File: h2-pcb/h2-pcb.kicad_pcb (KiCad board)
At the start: 2 copper layers, 123 x 74.8 mm, 102 parts, among them J1 Network Connector, J10 Temp Sensor Conn 3, J11 Actuator Connector 4, J12 Manometer Connector 3, J2 STDC14, J3 Manometer Connector 1, J4 Manometer Connector 2, J5 Actuator Connector 1, J6 Actuator Connector 2, J7 Actuator Connector 3, J8 Temp Sensor Conn 1, J9 Temp Sensor Conn 2, Q1 NMOS, Q2 PMOS, Q3 NMOS, Q4 PMOS, Q5 NMOS, Q6 PMOS, Q7 NMOS, Q8 PMOS, SW1 SW_Push, U1 LD39050PU33R, U2 STM32G474RBT6, U3 SN65HVD230, U4 DS2484, Y1 8MHz

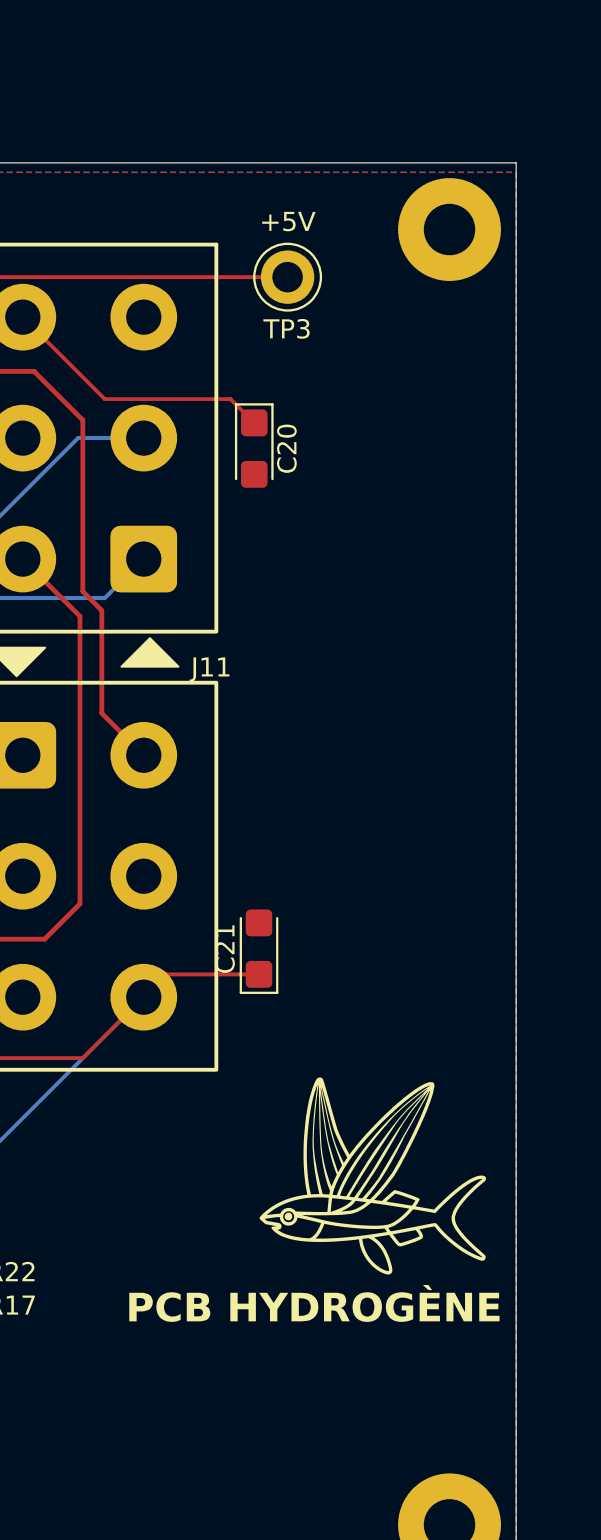
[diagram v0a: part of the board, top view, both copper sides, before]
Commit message: h2-pcb: update metadata and silkscreen
- Update author, pcb code, version and date metadata
- Add version and code to PCB name in silkscreen
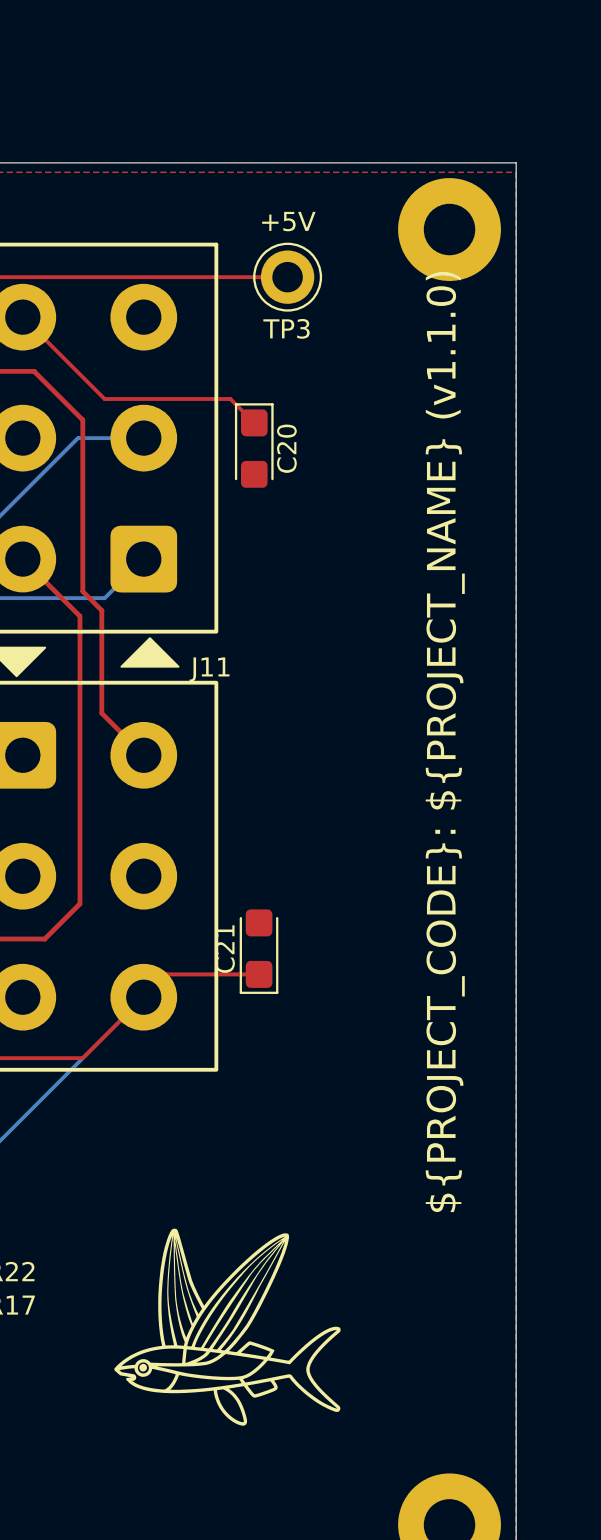
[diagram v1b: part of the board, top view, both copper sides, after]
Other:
- board text added: "${PROJECT_CODE}: ${PROJECT_NAME} (${REVISION})"
- board text removed: "PCB HYDROGÈNE"

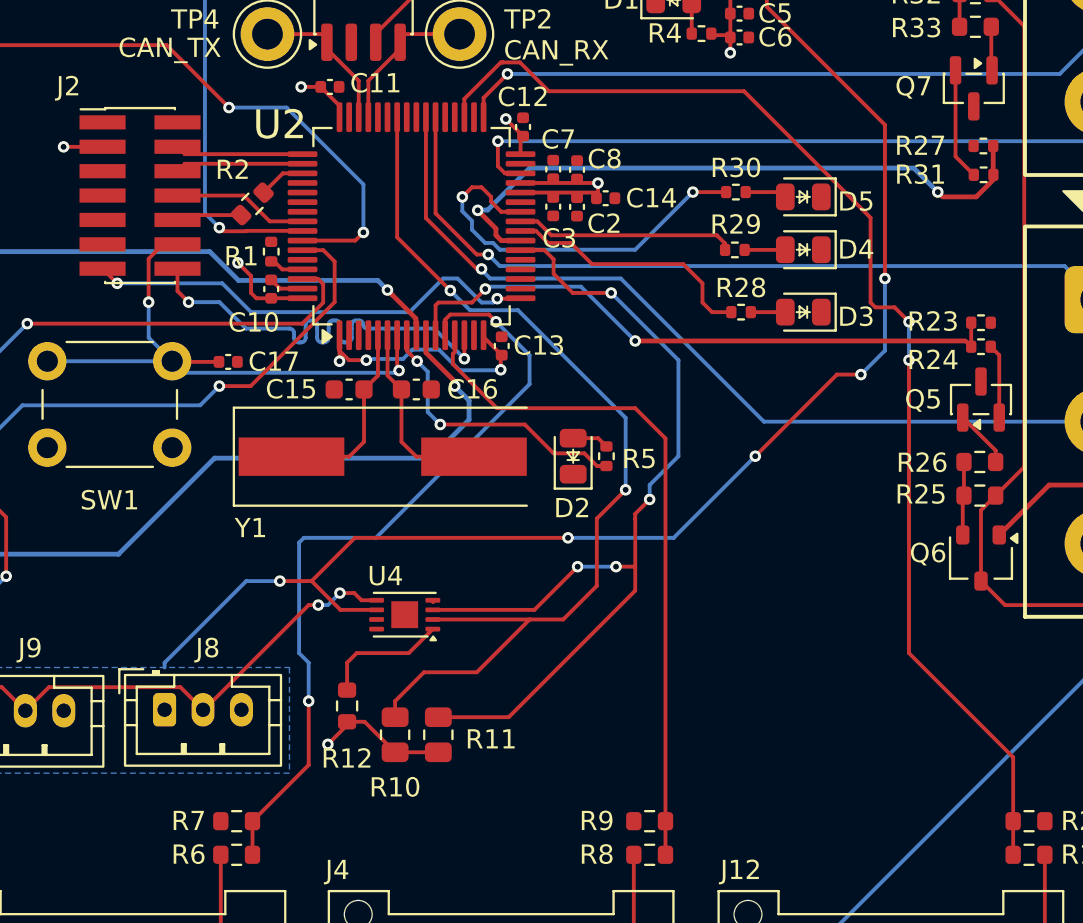
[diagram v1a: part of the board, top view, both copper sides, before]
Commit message: h2-pcb: make i2c traces parallel
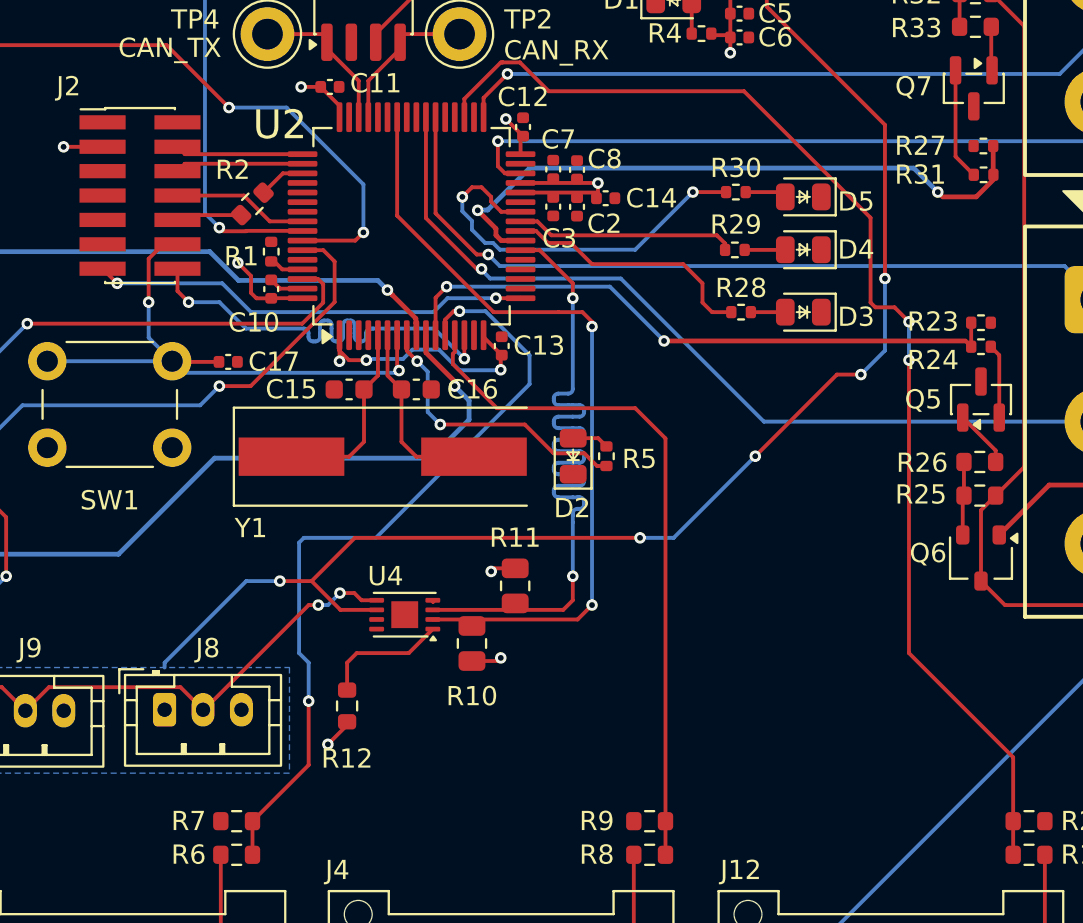
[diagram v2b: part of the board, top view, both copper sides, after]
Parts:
- moved R11 8.72 mm to (106.8, 95.0), turned to -90 degrees
- moved R10 6.21 mm to (104.5, 98.0)
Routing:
- net /SDA_TEMP: track 50.8 -> 40.9 mm
- net /SCL_TEMP: track 48.4 -> 40.8 mm, vias 4 -> 2
- net +3.3V: track 50.7 -> 48.0 mm, vias 11 -> 13
- net /STM32 Base Layout/T_VCP_RX: track 24.3 -> 23.3 mm
- net /STM32 Base Layout/T_VCP_TX: track 24.1 -> 23.2 mm

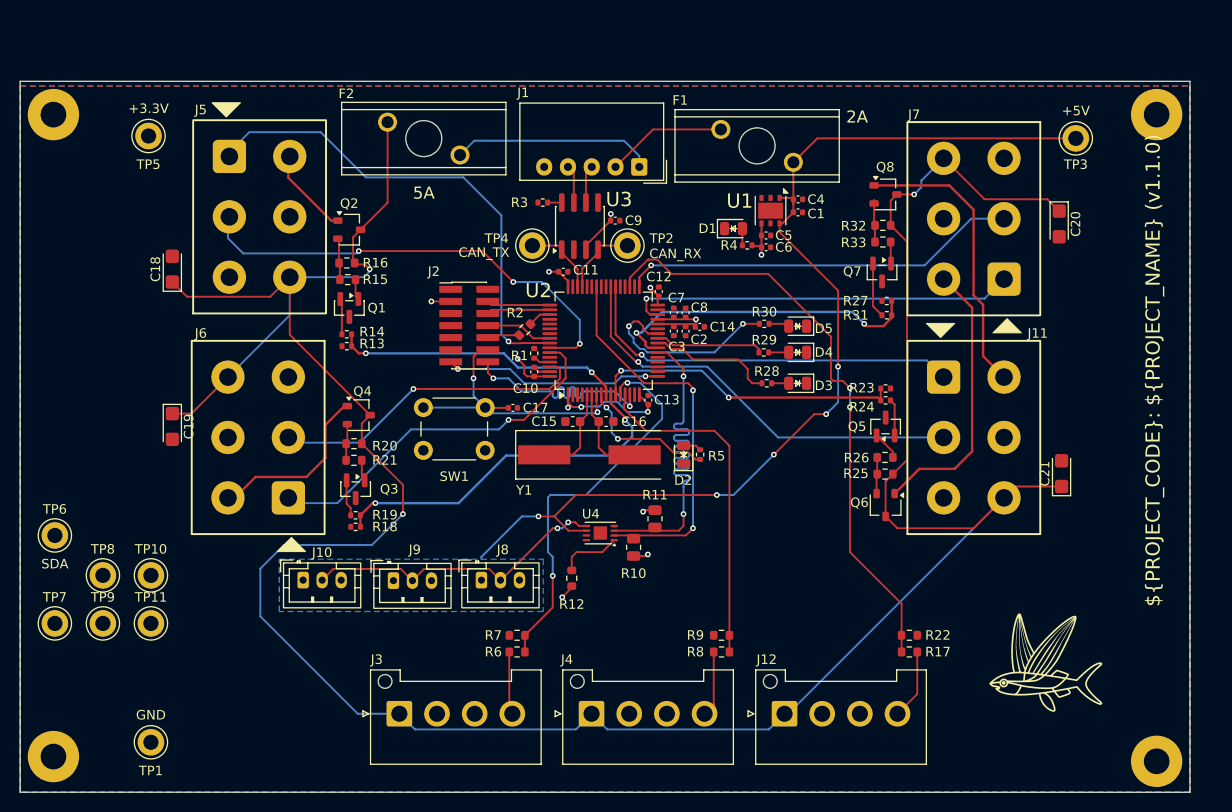
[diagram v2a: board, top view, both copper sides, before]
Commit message: Ajout des noms des composantes, routage des test points, 24V plane pour les manometres,  mounting holes 4mm de distance du edge
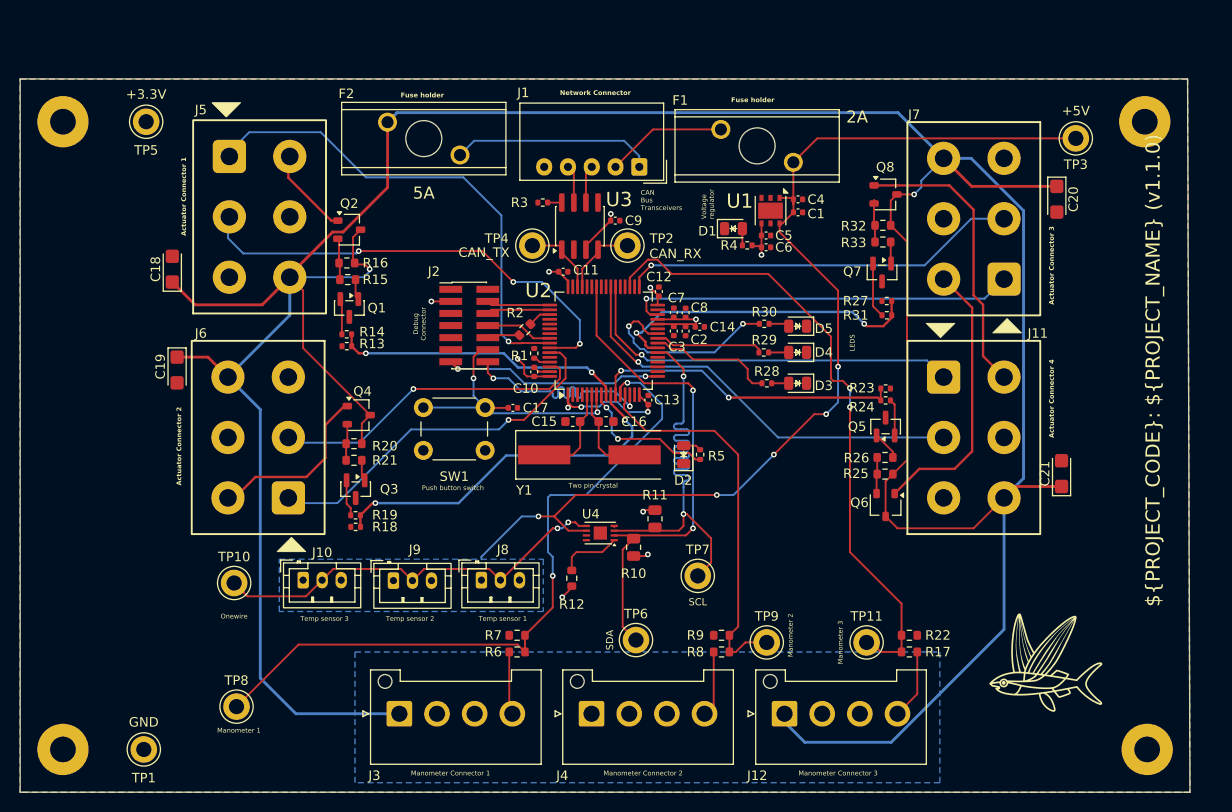
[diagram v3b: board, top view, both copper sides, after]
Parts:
- moved TP11 75.3 mm to (129.0, 108.0)
- moved TP9 69.8 mm to (118.5, 108.0)
- moved TP7 67.8 mm to (111.2, 101.0)
- moved TP6 62.1 mm to (104.8, 107.8)
- moved TP8 19.7 mm to (62.8, 114.8)
- moved TP10 8.79 mm to (62.5, 101.8)
- moved C19 5.96 mm to (56.5, 79.4)
- moved C20 2.61 mm to (149.0, 61.4)
- moved H3 1.60 mm to (158.5, 119.2)
- moved TP5 1.52 mm to (53.2, 53.2)
- moved H2 1.46 mm to (158.2, 53.2)
- moved H1 1.25 mm to (44.5, 53.2)
- moved H4 1.25 mm to (44.5, 119.2)
- moved TP1 1.06 mm to (53.0, 119.2)
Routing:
- net +24V: track 288.0 -> 364.0 mm, vias 3 -> 2
- net /MANOMETER_1: track 40.9 -> 74.7 mm
- net /SDA_TEMP: track 40.9 -> 52.6 mm
- net /ONEWIRE: track 32.4 -> 43.0 mm
- net /SCL_TEMP: track 40.8 -> 49.2 mm
- net /MANOMETER_2: track 35.9 -> 41.0 mm
- net /MANOMETER_3: track 63.1 -> 67.2 mm
- added copper zone on B.Cu, net +24V
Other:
- board size 123 x 74.8 mm -> 123 x 75 mm
- board text added: "Actuator Connector 1"
- board text added: "Actuator Connector 2"
- board text added: "Actuator Connector 3"
- board text added: "Actuator Connector 4"
- board text added: "CAN Bus Transceivers"
- board text added: "Debug Connector"
- board text added: "Fuse holder"
- board text added: "LEDS"
- board text added: "Manometer 1"
- board text added: "Manometer 2"
- board text added: "Manometer 3"
- board text added: "Manometer Connector 1"
- board text added: "Manometer Connector 2"
- board text added: "Manometer Connector 3"
- board text added: "Network Connector"
- board text added: "Onewire"
- board text added: "Push button switch"
- board text added: "SCL"
- board text added: "SDA"
- board text added: "Temp sensor 1"
- board text added: "Temp sensor 2"
- board text added: "Temp sensor 3"
- board text added: "Two pin crystal"
- board text added: "Voltage regulator"

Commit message: h2-pcb: replace ds2484 symbol
The symbol is now the one from the official KiCad library. PCB was also
updated and any remaining DRC errors were fixed.
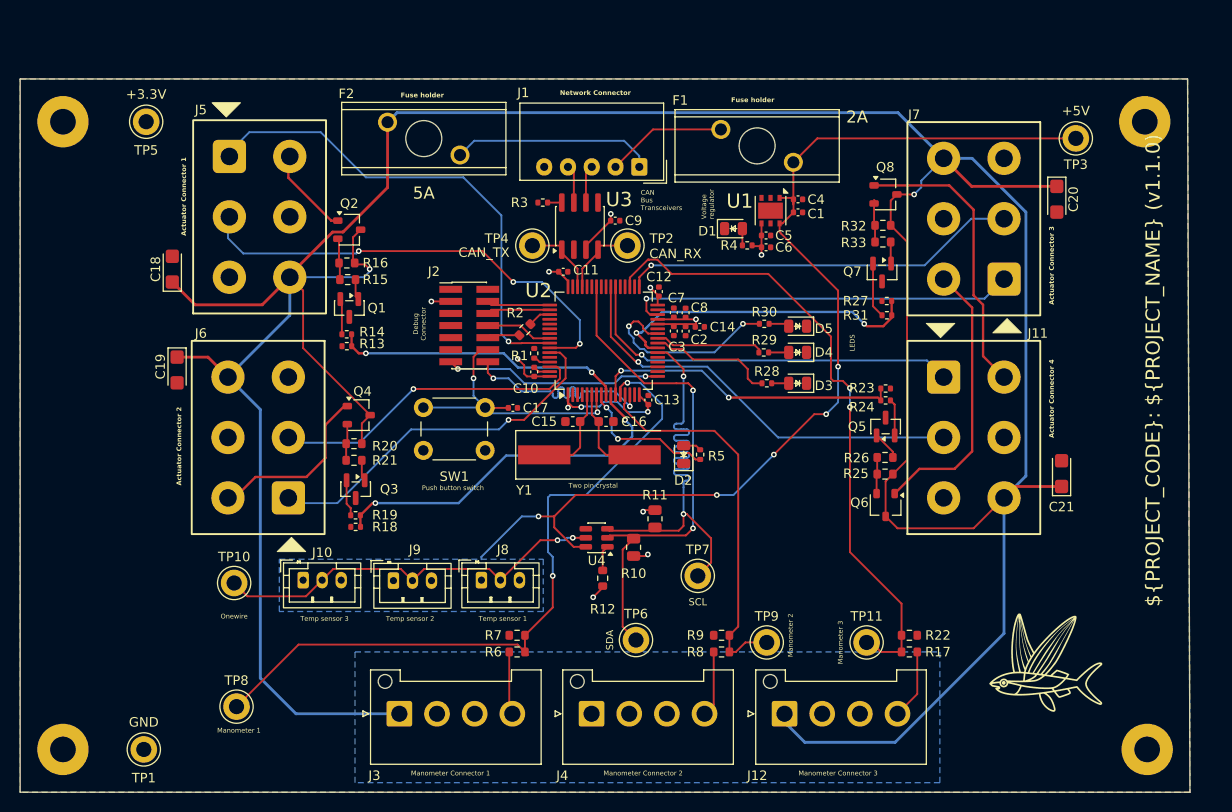
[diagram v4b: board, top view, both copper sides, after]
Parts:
- U4: value DS2484 -> DS2484R; footprint Package_DFN_QFN:TDFN-8-1EP_3x2mm_P0.5mm_EP1.4x1.4mm -> Package_TO_SOT_SMD:SOT-23-6
- moved R12 3.25 mm to (101.2, 101.2), turned to 90 degrees
- moved U4 0.63 mm to (100.6, 97.0)
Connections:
- R12 pad 1: Net-(U4-SLPZ) -> +3.3V
- R12 pad 2: +3.3V -> Net-(U4-~{SLPZ})
- U4 pad 1: Net-(U4-SLPZ) -> Net-(U4-~{SLPZ})
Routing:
- net Net-(U4-SLPZ): track 6.69 -> 0.00 mm
- net Net-(U4-~{SLPZ}): track 0.00 -> 2.76 mm
- net +5V: track 110.4 -> 111.7 mm
- net /ONEWIRE: track 43.0 -> 42.1 mm
- net /SDA_TEMP: track 52.6 -> 53.4 mm
- net /SCL_TEMP: track 49.2 -> 50.0 mm
- net +24V: track 364.0 -> 364.5 mm

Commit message: h2-pcb: implement review comments
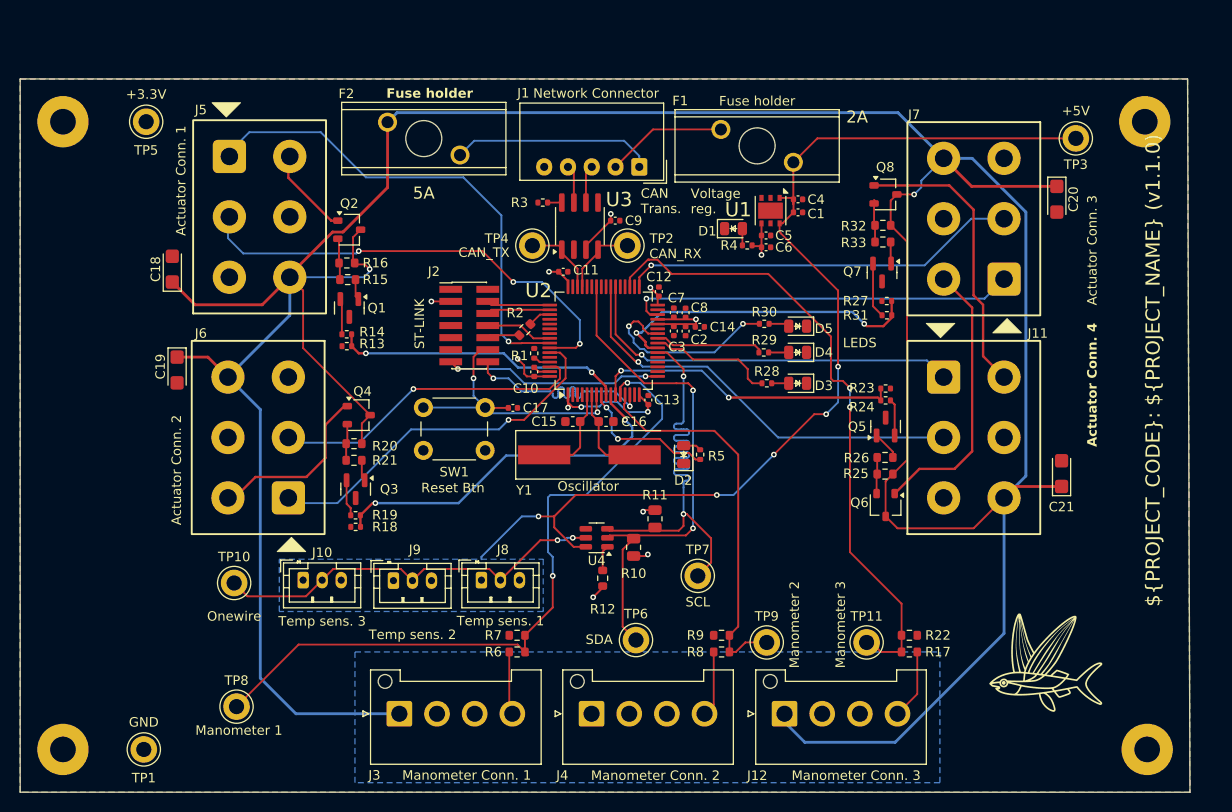
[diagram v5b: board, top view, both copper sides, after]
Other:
- board text added: "Actuator Conn. 1"
- board text added: "Actuator Conn. 2"
- board text added: "Actuator Conn. 3"
- board text added: "Actuator Conn. 4"
- board text added: "CAN Trans."
- board text added: "Manometer Conn. 1"
- board text added: "Manometer Conn. 2"
- board text added: "Manometer Conn. 3"
- board text added: "Oscillator"
- board text added: "Reset Btn"
- board text added: "ST-LINK"
- board text added: "Temp sens. 1"
- board text added: "Temp sens. 2"
- board text added: "Temp sens. 3"
- board text added: "Voltage reg."
- board text removed: "Actuator Connector 1"
- board text removed: "Actuator Connector 2"
- board text removed: "Actuator Connector 3"
- board text removed: "Actuator Connector 4"
- board text removed: "CAN Bus Transceivers"
- board text removed: "Debug Connector"
- board text removed: "Manometer Connector 1"
- board text removed: "Manometer Connector 2"
- board text removed: "Manometer Connector 3"
- board text removed: "Push button switch"
- board text removed: "Temp sensor 1"
- board text removed: "Temp sensor 2"
- board text removed: "Temp sensor 3"
- board text removed: "Two pin crystal"
- board text removed: "Voltage regulator"
